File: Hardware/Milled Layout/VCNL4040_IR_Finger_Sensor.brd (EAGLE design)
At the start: 20.4 x 17.8 mm, 9 parts, among them U1 VCNL4040

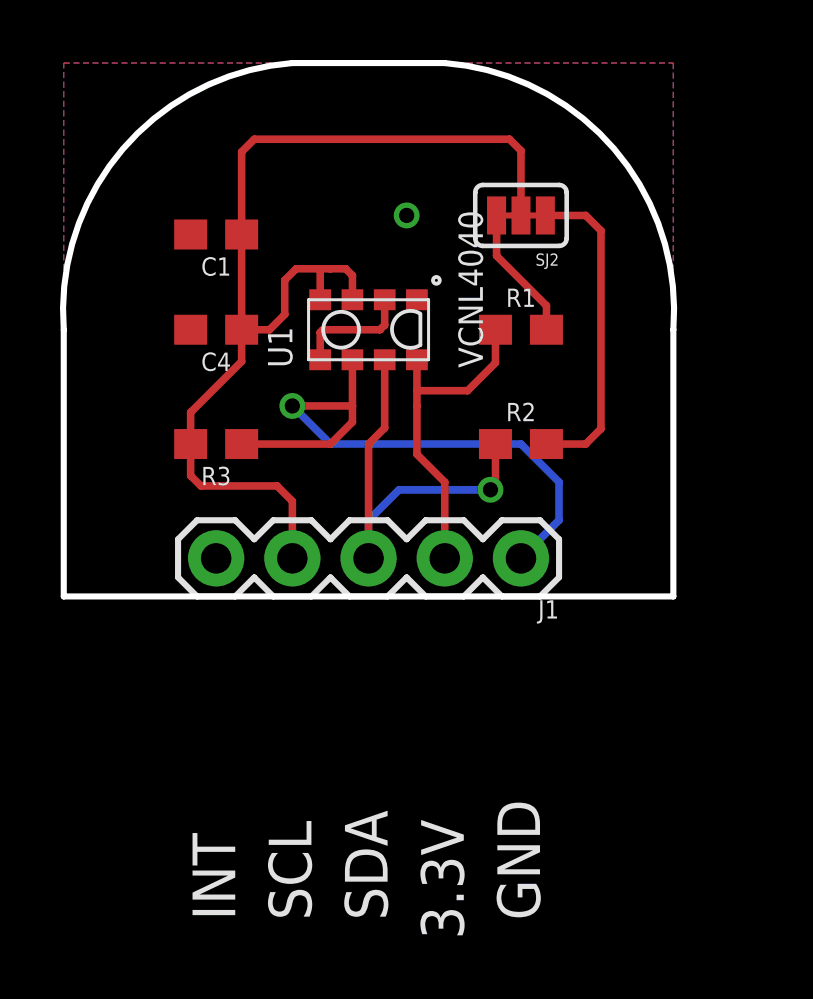
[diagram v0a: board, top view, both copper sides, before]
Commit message: Got rid of INT pin for Mill version
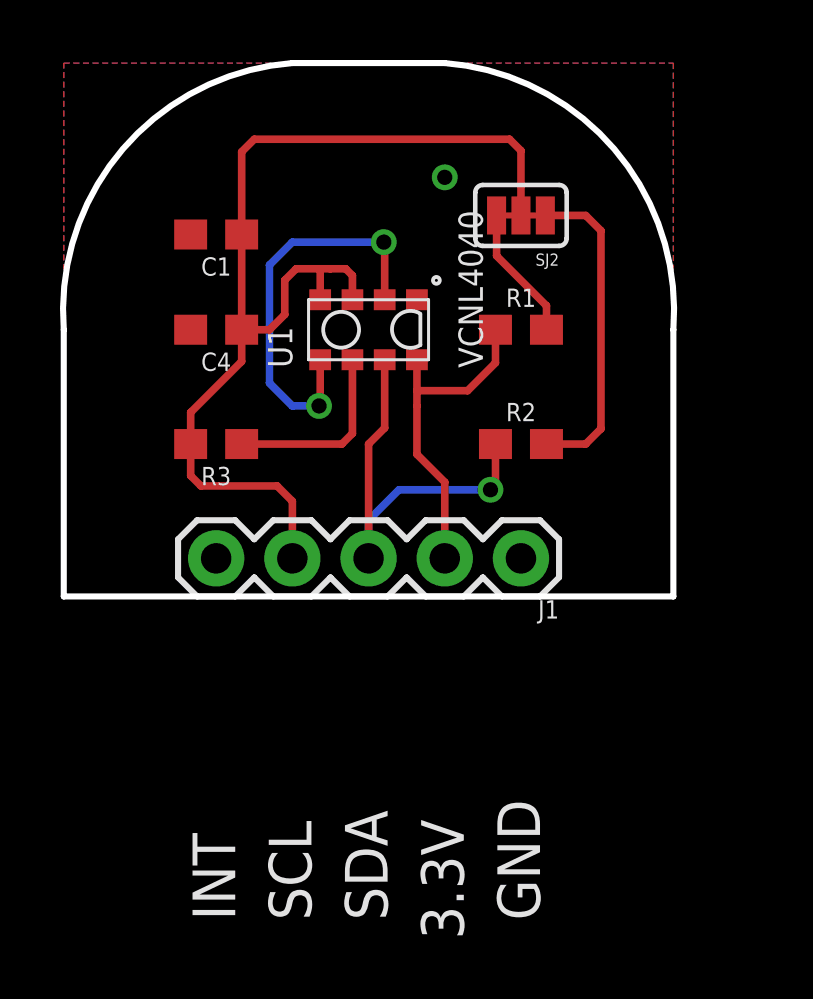
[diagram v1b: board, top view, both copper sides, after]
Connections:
- net INT: no longer J1.1
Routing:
- net INT: track 21.1 -> 6.30 mm, vias 1 -> 0
- net N$1: track 4.01 -> 13.5 mm, vias 0 -> 2
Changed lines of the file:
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@@
 <vertex x="17.78" y="0"/>
 </polygon>
-<via x="8.89" y="12.7" extent="1-16" drill="0.508"/>
+<via x="10.16" y="13.97" extent="1-16" drill="0.508"/>
 </signal>
 <signal name="SCL">
@@
 <contactref element="U1" pad="6"/>
 <contactref element="R3" pad="1"/>
-<contactref element="J1" pad="1"/>
-<wire x1="3.39" y1="5.08" x2="6.35" y2="5.08" width="0.254" layer="1"/>
-<wire x1="6.35" y1="5.08" x2="7.0825" y2="5.8125" width="0.254" layer="1"/>
-<wire x1="7.0825" y1="5.8125" x2="7.0825" y2="6.35" width="0.254" layer="1"/>
-<wire x1="7.0825" y1="6.35" x2="7.0825" y2="7.89" width="0.254" layer="1"/>
-<wire x1="12.7" y1="1.27" x2="13.97" y2="2.54" width="0.254" layer="16"/>
-<wire x1="13.97" y1="2.54" x2="13.97" y2="3.81" width="0.254" layer="16"/>
-<wire x1="13.97" y1="3.81" x2="12.7" y2="5.08" width="0.254" layer="16"/>
-<wire x1="12.7" y1="5.08" x2="6.35" y2="5.08" width="0.254" layer="16"/>
-<wire x1="6.35" y1="5.08" x2="5.08" y2="6.35" width="0.254" layer="16"/>
-<via x="5.08" y="6.35" extent="1-16" drill="0.508"/>
-<wire x1="5.08" y1="6.35" x2="7.0825" y2="6.35" width="0.254" layer="1"/>
+<wire x1="3.39" y1="5.08" x2="6.731" y2="5.08" width="0.254" layer="1"/>
+<wire x1="7.0825" y1="5.4315" x2="7.0825" y2="7.89" width="0.254" layer="1"/>
+<wire x1="7.0825" y1="5.4315" x2="6.731" y2="5.08" width="0.254" layer="1"/>
 </signal>
 <signal name="3.3V">
@@
 <contactref element="U1" pad="5"/>
 <contactref element="U1" pad="2"/>
-<wire x1="6.0075" y1="7.89" x2="6.0075" y2="8.8015" width="0.254" layer="1"/>
-<wire x1="6.0075" y1="8.8015" x2="6.096" y2="8.89" width="0.254" layer="1"/>
-<wire x1="6.096" y1="8.89" x2="8.001" y2="8.89" width="0.254" layer="1"/>
-<wire x1="8.001" y1="8.89" x2="8.1575" y2="9.0465" width="0.254" layer="1"/>
-<wire x1="8.1575" y1="9.0465" x2="8.1575" y2="9.89" width="0.254" layer="1"/>
+<wire x1="8.1575" y1="9.89" x2="8.1575" y2="11.7815" width="0.254" layer="1"/>
+<wire x1="8.1575" y1="11.7815" x2="8.128" y2="11.811" width="0.254" layer="1"/>
+<via x="8.128" y="11.811" extent="1-16" drill="0.508"/>
+<wire x1="8.128" y1="11.811" x2="5.08" y2="11.811" width="0.254" layer="16"/>
+<wire x1="5.08" y1="11.811" x2="4.318" y2="11.049" width="0.254" layer="16"/>
+<wire x1="4.318" y1="11.049" x2="4.318" y2="7.112" width="0.254" layer="16"/>
+<wire x1="4.318" y1="7.112" x2="5.08" y2="6.35" width="0.254" layer="16"/>
+<wire x1="5.08" y1="6.35" x2="5.969" y2="6.35" width="0.254" layer="16"/>
+<via x="5.969" y="6.35" extent="1-16" drill="0.508"/>
+<wire x1="5.969" y1="6.35" x2="6.0075" y2="6.3885" width="0.254" layer="1"/>
+<wire x1="6.0075" y1="6.3885" x2="6.0075" y2="7.89" width="0.254" layer="1"/>
 </signal>
 </signals>

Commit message: Moved larger board back to origin
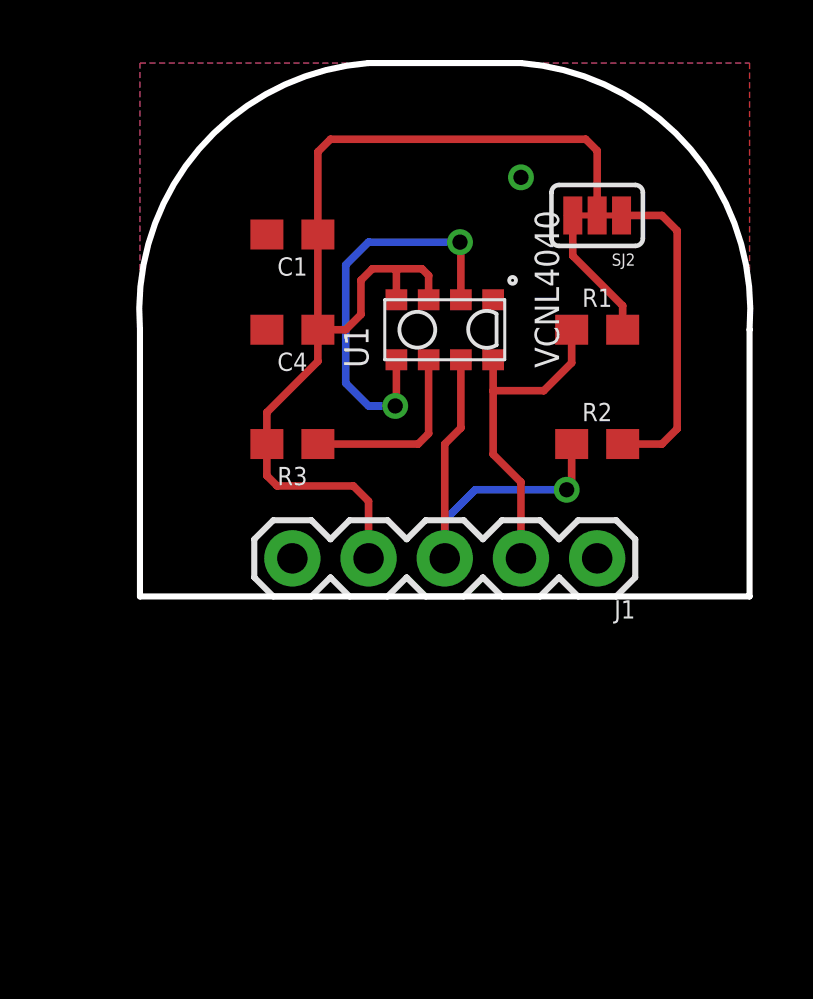
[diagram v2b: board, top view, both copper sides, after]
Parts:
- moved J1 2.54 mm to (15.2, 1.27)
- moved R1 2.54 mm to (15.2, 8.89)
- moved R2 2.54 mm to (15.2, 5.08)
- moved SJ2 2.54 mm to (15.2, 12.7)
- moved C1 2.54 mm to (5.08, 12.1)
- moved C4 2.54 mm to (5.08, 8.89)
- moved R3 2.54 mm to (5.08, 5.08)
- moved U1 2.54 mm to (10.2, 8.89)
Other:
- board text removed: "3.3V"
- board text removed: "GND"
- board text removed: "INT"
- board text removed: "SCL"
- board text removed: "SDA"
